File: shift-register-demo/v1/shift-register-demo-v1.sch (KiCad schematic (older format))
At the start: 28 parts

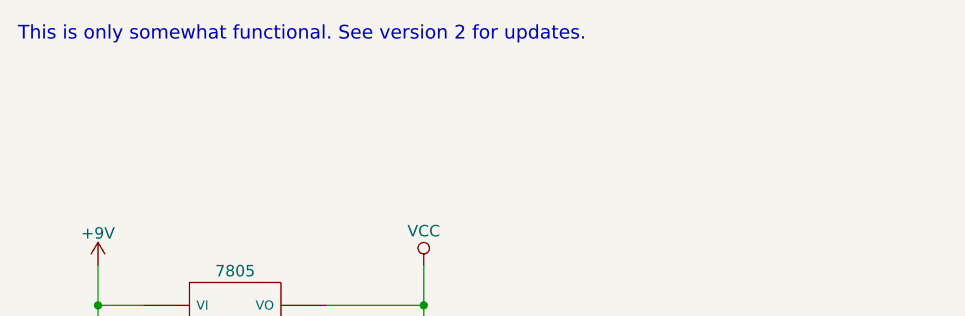
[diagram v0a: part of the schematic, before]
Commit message: Added v1 schematic pdf.
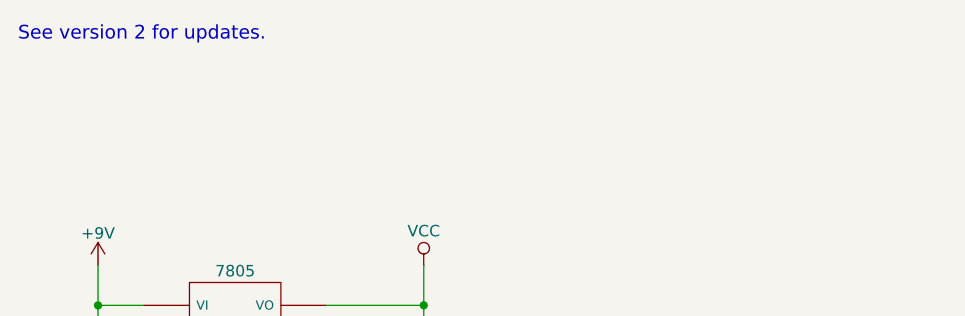
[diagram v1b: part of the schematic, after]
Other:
- note added: "See version 2 for updates."
- note removed: "This is only somewhat functional. See version 2 for updates."
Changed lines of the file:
@@
 LIBS:wicker-linear
 LIBS:74xx
-LIBS:shift-register-demo-cache
 EELAYER 25 0
 EELAYER END
@@
 $EndComp
 Text Notes 900  725  0    60   ~ 0
-This is only somewhat functional. See version 2 for updates.
+See version 2 for updates.
 Text Label 1300 3675 0    60   ~ 0
 DATA_IN
